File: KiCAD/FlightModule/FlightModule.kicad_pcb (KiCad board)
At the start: 2 copper layers, 90 x 70 mm, 72 parts, among them J1 DF11B-8DP-2DS, J4 DF51-2P-2DS, J5 DF51A-4P-2DSA, Q1 AO3400A, Q2 AO3400A, Q3 2SC3325-Y, U1 MB85RQ8MX, U2 MB85RQ8MX, U3 SAM-M8Q-0-10, U4 MB85RQ8MX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

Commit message: 最終確認終わり
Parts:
- added C1: 330uF, Capacitor_SMD:CP_Elec_10x10, F.Cu at (183.9, 114.6)
- added D5: GS1010FL, Diode_SMD:D_SOD-123F, F.Cu at (191.5, 111.0)
- added G***: LOGO, LOGO, B.Cu at (136.4, 132.2)
- added G***: LOGO, LOGO, B.Cu at (162.4, 131.5)
- C10, C11: value 1u -> 1uF; footprint Capacitor_SMD:C_0603_1608Metric_Pad1.08x0.95mm_HandSolder -> Capacitor_SMD:C_0805_2012Metric_Pad1.18x1.45mm_HandSolder; moved to B.Cu
- C16, C17: footprint Capacitor_SMD:C_1206_3216Metric_Pad1.33x1.80mm_HandSolder -> Capacitor_SMD:C_0805_2012Metric_Pad1.18x1.45mm_HandSolder
- C8, R25: moved to F.Cu
- D4: value R -> Green
- R15, R18: value 300 -> 300R
- R16, R19: value 10k -> 10kR
- R17, R20: value 2.4k -> 2.4kR
- R27: value 100k -> 100kR
- R28: value 0 -> 0R
- R29, R30: value 4.7k -> 4.7kR
- U5: moved to B.Cu
- moved PS1 8.71 mm to (182.9, 105.3)
- moved R25 6.26 mm to (134.1, 119.3), turned to 0 degrees
- moved C11 4.55 mm to (187.5, 94.6), turned to 0 degrees
- moved C10 4.55 mm to (187.5, 101.0), turned to 0 degrees
- moved C9 4.45 mm to (138.7, 114.0), turned to 180 degrees
- moved U5 4.32 mm to (185.4, 97.8)
- moved U7 4.02 mm to (136.4, 116.6)
- moved D1 2.17 mm to (145.0, 129.9)
- moved D12 2.17 mm to (155.6, 129.9)
- moved D2 2.17 mm to (147.3, 129.9)
- moved D3 2.17 mm to (150.4, 129.9)
- moved D7 2.17 mm to (153.4, 129.9)
- moved R24 2.11 mm to (134.1, 114.0)
- moved C8 1.88 mm to (138.7, 119.3), turned to 180 degrees
- moved BZ1 1.79 mm to (183.1, 87.9)
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- renumbered H1 to M3, H2 to M3, H4 to M3, H3 to M3
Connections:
- PS1 pad 1: +12V -> Net-(D5-K)
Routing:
- net +5V: track 108.2 -> 123.1 mm, vias 2 -> 0
- net Net-(D5-K): track 0.00 -> 10.4 mm
- net +12V: track 174.5 -> 181.0 mm, vias 5 -> 6
- net FLIGHT_PIN: track 29.0 -> 24.0 mm
- net Net-(C8-Pad2): track 13.6 -> 10.2 mm, vias 1 -> 2
- net +3.3V: track 300.8 -> 298.2 mm, vias 5 -> 7
- net Net-(D12-A): track 15.0 -> 12.9 mm
- net Net-(D7-A): track 15.0 -> 12.8 mm
- net Net-(D3-A): track 15.0 -> 12.8 mm
- net Net-(D2-A): track 15.0 -> 12.8 mm
- net Net-(D1-A): track 15.0 -> 12.8 mm
- net Net-(J4-Pin_2): track 17.0 -> 16.9 mm, vias 1 -> 0
- net GND: vias 20 -> 79
- added copper zone on B.Cu, net +3.3V
- added copper zone on B.Cu, net +5V
- removed copper zone on F.Cu, net +3.3V
- removed copper zone on F.Cu, net +5V
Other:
- board text added: "BUS"
- board text added: "BUZZER"
- board text added: "FLIGHT PIN"
- board text added: "Flight Module Build-1"
- board text added: "III"
- board text added: "IV"
- board text added: "MKR WAN 1310"
- board text added: "ON"
- board text added: "SUBARU"
- board text added: "Tokai Student Rocket Project"
- board text added: "V1.3"
- board text added: "不知火"
- board text removed: "ぶざー"

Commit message: 最終確認終わり
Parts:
- moved M3 5.83 mm to (120.0, 72.0)
- moved M3 5.83 mm to (120.0, 128.0)
- moved M3 5.83 mm to (180.0, 72.0)
- moved M3 5.83 mm to (180.0, 128.0)
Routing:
- net +3.3V: track 298.2 -> 296.9 mm
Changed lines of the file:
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@@
 	)
 	(footprint "MountingHole:MountingHole_3.2mm_M3_Pad_TopBottom"
-		(locked yes)
 		(layer "F.Cu")
-		(at 125 75)
+		(at 120 72)
 		(descr "Mounting Hole 3.2mm, M3")
 		(tags "mounting hole 3.2mm m3")
@@
 	)
 	(footprint "MountingHole:MountingHole_3.2mm_M3_Pad_TopBottom"
-		(locked yes)
 		(layer "F.Cu")
-		(at 125 125)
+		(at 120 128)
 		(descr "Mounting Hole 3.2mm, M3")
 		(tags "mounting hole 3.2mm m3")
@@
 	)
 	(footprint "MountingHole:MountingHole_3.2mm_M3_Pad_TopBottom"
-		(locked yes)
 		(layer "F.Cu")
-		(at 175 75)
+		(at 180 72)
 		(descr "Mounting Hole 3.2mm, M3")
 		(tags "mounting hole 3.2mm m3")
@@
 	)
 	(footprint "MountingHole:MountingHole_3.2mm_M3_Pad_TopBottom"
-		(locked yes)
 		(layer "F.Cu")
-		(at 175 125)
+		(at 180 128)
 		(descr "Mounting Hole 3.2mm, M3")
 		(tags "mounting hole 3.2mm m3")
@@
 	)
 	(gr_circle
-		(center 175 125)
-		(end 181.5 125)
+		(center 120 72)
+		(end 113 72)
 		(stroke
 			(width 0.1)
@@
 	)
 	(gr_circle
-		(center 125 125)
-		(end 118.4 125)
+		(center 120 128)
+		(end 113 128)
 		(stroke
 			(width 0.1)
@@
 	)
 	(gr_circle
-		(center 175 75)
-		(end 181.5 75)
+		(center 180 72)
+		(end 187 72)
 		(stroke
 			(width 0.1)
@@
 	)
 	(gr_circle
-		(center 125 75)
-		(end 131.5 75)
+		(center 180 128)
+		(end 187 128)
 		(stroke
 			(width 0.1)
@@
 	)
 	(segment
-		(start 185.42 119.38)
-		(end 185.42 122.555)
+		(start 180.467 119.38)
+		(end 174.879 124.968)
 		(width 1)
 		(layer "B.Cu")
@@
 	)
 	(segment
-		(start 185.42 122.555)
-		(end 177.673 130.302)
-		(width 1)
-		(layer "B.Cu")
-		(net 4)
-	)
-	(segment
-		(start 177.673 130.302)
-		(end 172.593 130.302)
-		(width 1)
-		(layer "B.Cu")
-		(net 4)
-	)
-	(segment
 		(start 172.085 131.318)
 		(end 172.593 130.81)
@@
 	)
 	(segment
+		(start 174.879 128.016)
+		(end 172.593 130.302)
+		(width 1)
+		(layer "B.Cu")
+		(net 4)
+	)
+	(segment
+		(start 174.879 124.968)
+		(end 174.879 128.016)
+		(width 1)
+		(layer "B.Cu")
+		(net 4)
+	)
+	(segment
 		(start 158.75 122.682)
 		(end 159.5 123.432)
@@
 	)
 	(segment
+		(start 185.42 119.38)
+		(end 180.467 119.38)
+		(width 1)
+		(layer "B.Cu")
+		(net 4)
+	)
+	(segment
 		(start 137.544 85.341)
 		(end 137.544 78.232)
@@
 	)
 	(segment
-		(start 186.436 78.994)
-		(end 177.8 70.358)
+		(start 175.006 73.533)
+		(end 178.689 77.216)
 		(width 0.4)
 		(layer "F.Cu")
@@
 	)
 	(segment
+		(start 186.436 82.169)
+		(end 186.436 90.678)
+		(width 0.4)
+		(layer "F.Cu")
+		(net 13)
+	)
+	(segment
 		(start 175.387 105.791)
 		(end 175.387 108.839)
@@
 	)
 	(segment
+		(start 178.689 77.216)
+		(end 181.483 77.216)
+		(width 0.4)
+		(layer "F.Cu")
+		(net 13)
+	)
+	(segment
+		(start 166.37 70.358)
+		(end 172.847 70.358)
+		(width 0.4)
+		(layer "F.Cu")
+		(net 13)
+	)
+	(segment
+		(start 181.483 77.216)
+		(end 186.436 82.169)
+		(width 0.4)
+		(layer "F.Cu")
+		(net 13)
+	)
+	(segment
 		(start 167.92 79.878)
 		(end 166.62 79.878)
@@
 	)
 	(segment
+		(start 172.847 70.358)
+		(end 175.006 72.517)
+		(width 0.4)
+		(layer "F.Cu")
+		(net 13)
+	)
+	(segment
 		(start 138.11 114.2725)
 		(end 137.8375 114)
@@
 	)
 	(segment
-		(start 186.436 90.678)
-		(end 186.436 78.994)
-		(width 0.4)
-		(layer "F.Cu")
-		(net 13)
-	)
-	(segment
 		(start 162.4095 66.6515)
 		(end 163.83 68.072)
@@
 	)
 	(segment
-		(start 177.8 70.358)
-		(end 166.37 70.358)
+		(start 175.006 72.517)
+		(end 175.006 73.533)
 		(width 0.4)
 		(layer "F.Cu")
@@
 		(layers "F.Cu" "B.Cu")
 		(hatch edge 0.5)
-		(connect_pads
+		(connect_pads yes
 			(clearance 0.3)
 		)

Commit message: ガバーデータ生成
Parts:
- moved G*** 3.71 mm to (132.8, 131.4), turned to 180 degrees
- moved J4 1.57 mm to (135.8, 134.1)
- renumbered M3 to H1, M3 to H2, M3 to H3, M3 to H4
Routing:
- net Net-(J4-Pin_2): track 16.9 -> 15.1 mm
- net GND: vias 79 -> 117

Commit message: Flight Module のビルド2が完成
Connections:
- H1 pad 1: GND -> (no net)
- H2 pad 1: GND -> (no net)
- H3 pad 1: GND -> (no net)
- H4 pad 1: GND -> (no net)
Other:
- board text added: "Flight Module Build-2"
- board text removed: "Flight Module Build-1"
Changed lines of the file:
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@@
 			)
 		)
-		(property "Description" "Mounting Hole with connection"
+		(property "Description" "Mounting Hole without connection"
 			(at 0 0 0)
 			(unlocked yes)
@@
 			)
 		)
-		(property ki_fp_filters "MountingHole*Pad*")
+		(property ki_fp_filters "MountingHole*")
 		(sheetname "/")
 		(sheetfile "FlightModule.kicad_sch")
@@
 			(layers "*.Cu" "*.Mask")
 			(remove_unused_layers no)
-			(net 8 "GND")
-			(pinfunction "1")
-			(pintype "input")
 		)
 		(pad "1" connect circle
@@
 			(size 6.4 6.4)
 			(layers "F.Cu" "F.Mask")
-			(net 8 "GND")
-			(pinfunction "1")
-			(pintype "input")
 		)
 		(pad "1" connect circle
@@
 			(size 6.4 6.4)
 			(layers "B.Cu" "B.Mask")
-			(net 8 "GND")
-			(pinfunction "1")
-			(pintype "input")
 		)
 		(embedded_fonts no)
@@
 			)
 		)
-		(property "Description" "Mounting Hole with connection"
+		(property "Description" "Mounting Hole without connection"
 			(at 0 0 0)
 			(unlocked yes)
@@
 			)
 		)
-		(property ki_fp_filters "MountingHole*Pad*")
+		(property ki_fp_filters "MountingHole*")
 		(sheetname "/")
 		(sheetfile "FlightModule.kicad_sch")
@@
 			(layers "*.Cu" "*.Mask")
 			(remove_unused_layers no)
-			(net 8 "GND")
-			(pinfunction "1")
-			(pintype "input")
 		)
 		(pad "1" connect circle
@@
 			(size 6.4 6.4)
 			(layers "F.Cu" "F.Mask")
-			(net 8 "GND")
-			(pinfunction "1")
-			(pintype "input")
 		)
 		(pad "1" connect circle
@@
 			(size 6.4 6.4)
 			(layers "B.Cu" "B.Mask")
-			(net 8 "GND")
-			(pinfunction "1")
-			(pintype "input")
 		)
 		(embedded_fonts no)
@@
 			)
 		)
-		(property "Description" "Mounting Hole with connection"
+		(property "Description" "Mounting Hole without connection"
 			(at 0 0 0)
 			(unlocked yes)
@@
 			)
 		)
-		(property ki_fp_filters "MountingHole*Pad*")
+		(property ki_fp_filters "MountingHole*")
 		(sheetname "/")
 		(sheetfile "FlightModule.kicad_sch")
@@
 			(layers "*.Cu" "*.Mask")
 			(remove_unused_layers no)
-			(net 8 "GND")
-			(pinfunction "1")
-			(pintype "input")
 		)
 		(pad "1" connect circle
@@
 			(size 6.4 6.4)
 			(layers "F.Cu" "F.Mask")
-			(net 8 "GND")
-			(pinfunction "1")
-			(pintype "input")
 		)
 		(pad "1" connect circle
@@
 			(size 6.4 6.4)
 			(layers "B.Cu" "B.Mask")
-			(net 8 "GND")
-			(pinfunction "1")
-			(pintype "input")
 		)
 		(embedded_fonts no)
@@
 			)
 		)
-		(property "Description" "Mounting Hole with connection"
+		(property "Description" "Mounting Hole without connection"
 			(at 0 0 0)
 			(unlocked yes)
@@
 			)
 		)
-		(property ki_fp_filters "MountingHole*Pad*")
+		(property ki_fp_filters "MountingHole*")
 		(sheetname "/")
 		(sheetfile "FlightModule.kicad_sch")
@@
 			(layers "*.Cu" "*.Mask")
 			(remove_unused_layers no)
-			(net 8 "GND")
-			(pinfunction "1")
-			(pintype "input")
 		)
 		(pad "1" connect circle
@@
 			(size 6.4 6.4)
 			(layers "F.Cu" "F.Mask")
-			(net 8 "GND")
-			(pinfunction "1")
-			(pintype "input")
 		)
 		(pad "1" connect circle
@@
 			(size 6.4 6.4)
 			(layers "B.Cu" "B.Mask")
-			(net 8 "GND")
-			(pinfunction "1")
-			(pintype "input")
 		)
 		(embedded_fonts no)
@@
 		)
 	)
-	(gr_text "Flight Module  Build-1"
+	(gr_text "Flight Module  Build-2"
 		(at 158.623 134.239 0)
 		(layer "B.SilkS")

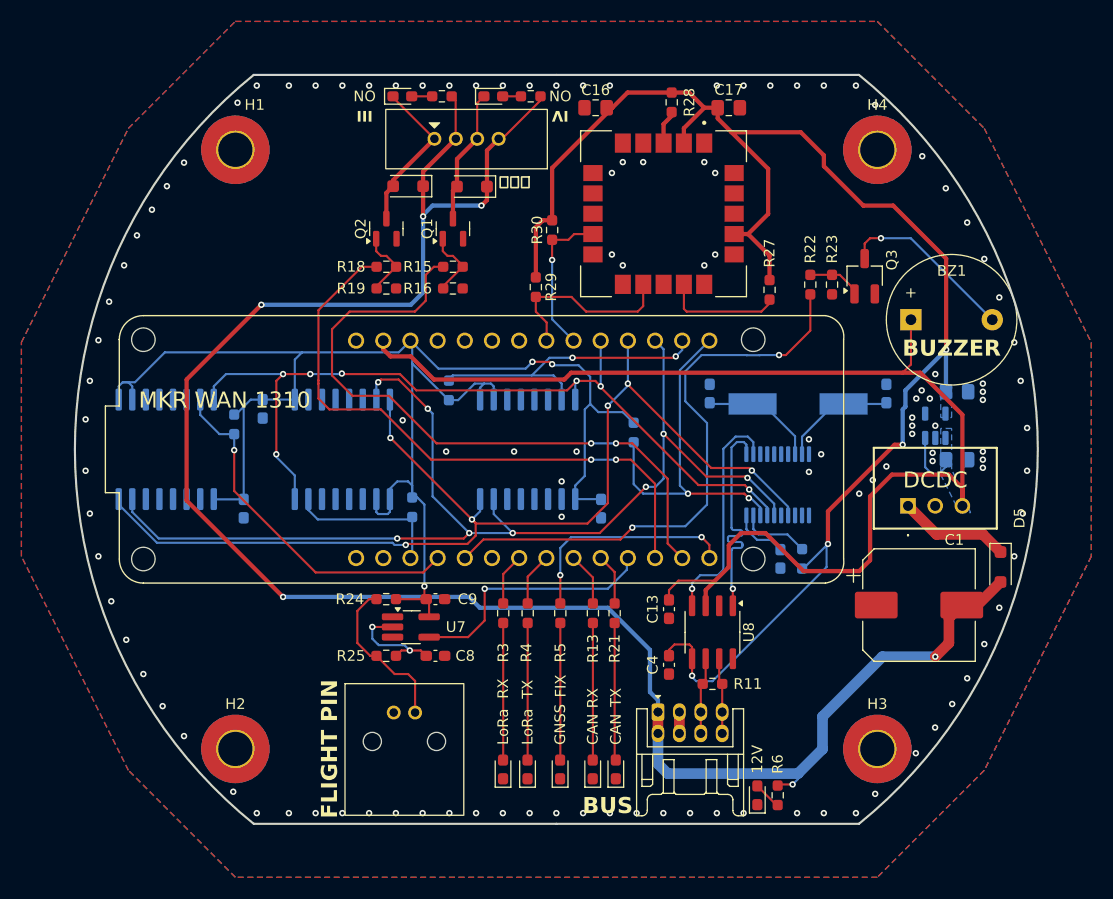
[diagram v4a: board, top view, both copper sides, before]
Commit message: Build-2完成．今回は発注しない．
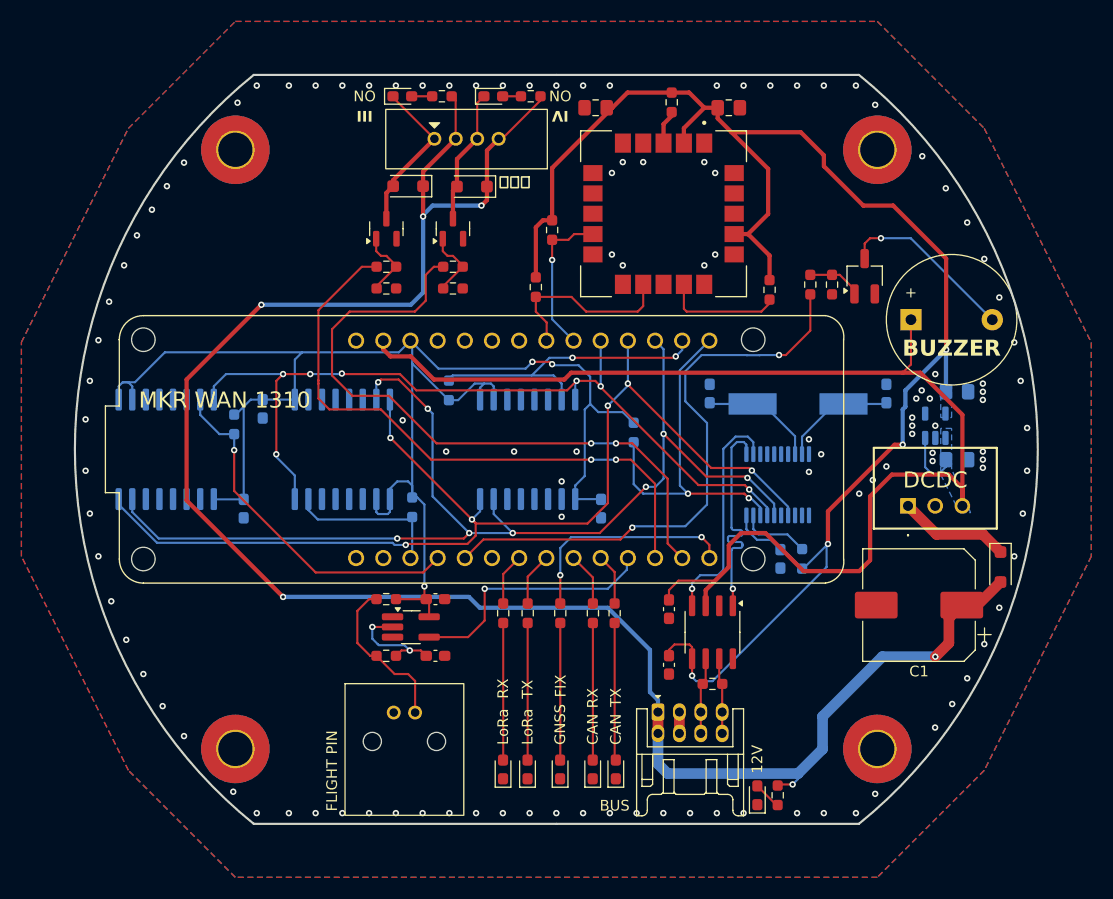
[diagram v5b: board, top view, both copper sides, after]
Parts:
- turned C1 to 180 degrees
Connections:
- C1 pad 1: GND -> +12V
- C1 pad 2: +12V -> GND
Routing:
- net GND: vias 117 -> 116
